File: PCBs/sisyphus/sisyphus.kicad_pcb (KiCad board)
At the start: 2 copper layers, 52 x 42 mm, 70 parts, among them J1 Light sensor, J10 Keyboard, J2 USB_C_Receptacle_USB2.0_14P, J3 AUX USB, J4 USB_BOOT, J5 Speaker, J6 Battery, J7 SWD, J8 Limit SW, J9 RGB_CONN, Q1 AO3401A, SW1 SW_SPDT_321, U1 TPS62293, U2 USBLC6-2P6, U3 BQ25619, U4 W25Q128JVS, U5 MAX98357A, U7 RP2040, Y1 ABM8-272-T3

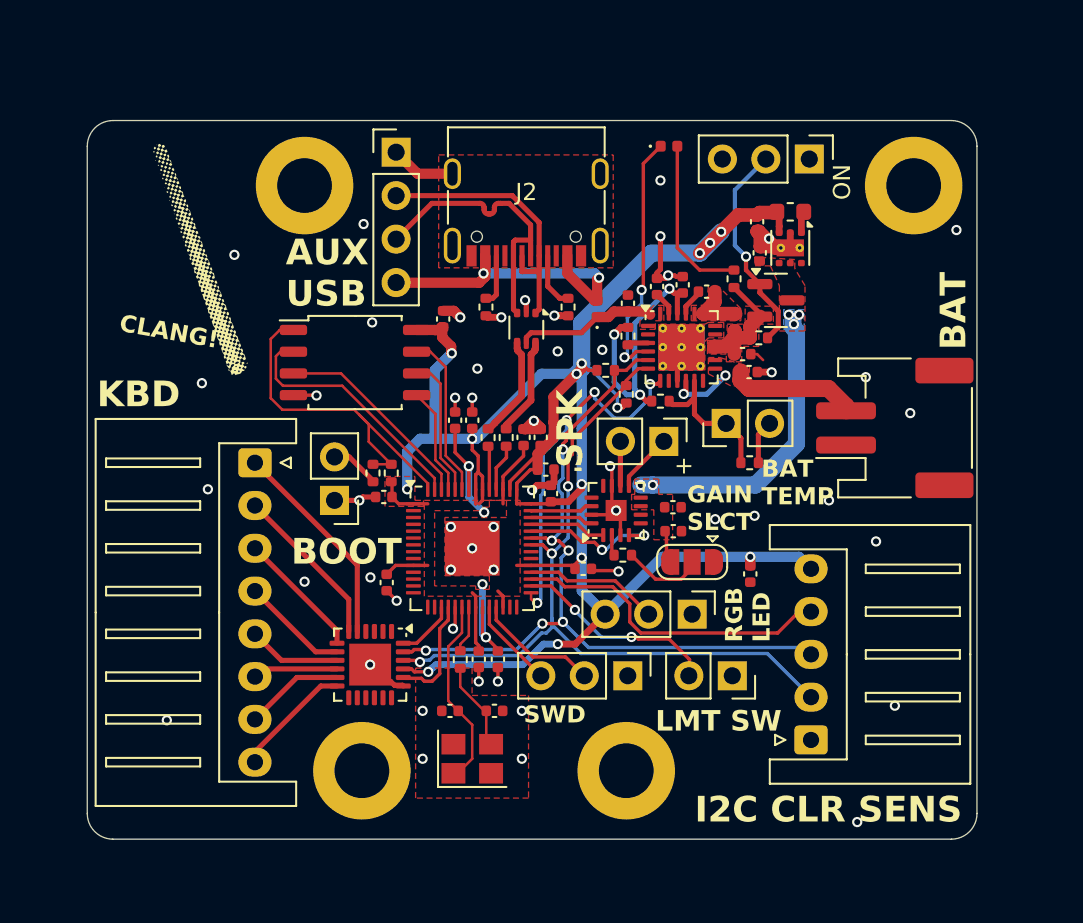
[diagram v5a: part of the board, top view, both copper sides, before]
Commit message: Fix things on PCB, update inductor size
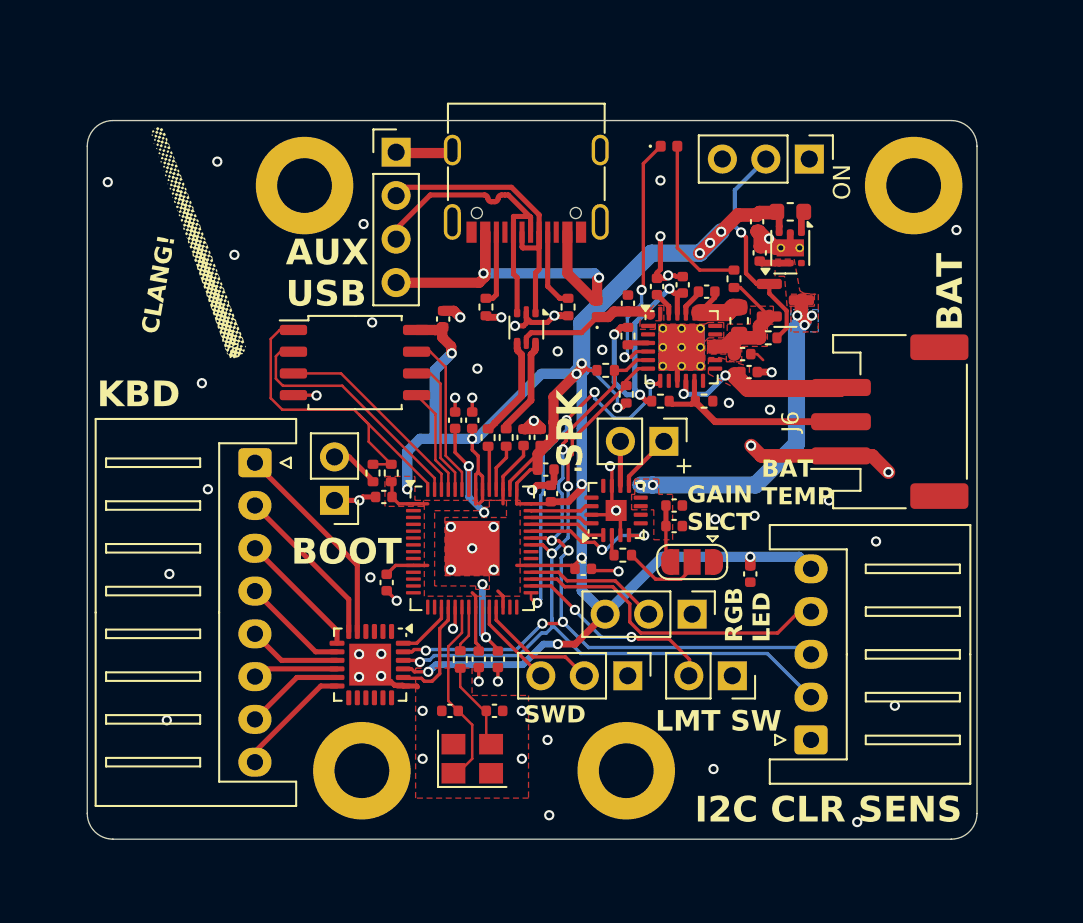
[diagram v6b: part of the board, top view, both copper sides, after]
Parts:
- removed TH1: 10k NTC, Connector_PinHeader_2.54mm:PinHeader_1x02_P2.54mm_Vertical
- J6: footprint Connector_JST:JST_PH_S2B-PH-SM4-TB_1x02-1MP_P2.00mm_Horizontal -> Connector_JST:JST_PH_S3B-PH-SM4-TB_1x03-1MP_P2.00mm_Horizontal
- L1: value 1uH -> 1uH 2A; footprint Inductor_SMD:L_0402_1005Metric -> Inductor_SMD:L_0603_1608Metric
- L2: value 2.2uH 1A -> 2.2uH 1.2A
- R8: value DNF -> 10k
- U8: value ~ -> TCA8418
- moved R7 4.48 mm to (113.5, 91.4)
- moved C10 1.50 mm to (111.8, 97.5)
- moved J2 1.38 mm to (103.2, 77.8)
- moved C9 1.10 mm to (111.8, 98.7)
- moved Q1 0.55 mm to (118.3, 85.5)
- moved R1 0.55 mm to (117.3, 87.7)
- moved J6 0.47 mm to (124.4, 92.6)
- moved L1 0.27 mm to (115.6, 86.7)
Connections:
- J6 pad 2: +BATT -> /Batery and power/NTC
- R6 pad 2: Net-(U3-TS) -> /Batery and power/NTC
- R7 pad 1: Net-(U3-TS) -> /Batery and power/NTC
- U3 pad 11: Net-(U3-TS) -> /Batery and power/NTC
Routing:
- net /Batery and power/NTC: track 0.00 -> 11.9 mm
- net GND: track 45.8 -> 55.3 mm, vias 52 -> 62
- net Net-(U3-TS): track 8.41 -> 0.00 mm
- net VSYS: track 19.4 -> 23.9 mm
- net VBUS: track 19.3 -> 23.4 mm
- net /Peripheral/DN: track 16.4 -> 17.8 mm
- net Net-(J2-CC1): track 3.26 -> 4.64 mm
- net Net-(J2-CC2): track 2.97 -> 4.35 mm
- net +BATT: track 11.2 -> 10.3 mm
- net SYS: track 8.74 -> 9.58 mm
- net /Peripheral/DP: track 17.1 -> 17.9 mm
- net Net-(Q1-G): track 12.5 -> 13.1 mm
- net /Batery and power/SW: track 3.49 -> 4.03 mm
- removed copper zone on F.Cu, net /Batery and power/SW

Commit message: Update things for that rendering F L A R E
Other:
- board text added: "NTC"
- board text removed: "BAT TEMP"

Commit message: Add the first actually ordered version of the PCB
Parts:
- removed the R6 at (111.0, 91.4)
- removed the R7 at (113.5, 91.4)
- added R11: 10k, Resistor_SMD:R_0402_1005Metric, F.Cu at (111.0, 91.3)
- D1: renamed from D2; footprint LED_SMD:LED_0402_1005Metric -> LED_SMD:LED_0603_1608Metric
- D2: renamed from D1; value D_Schottky -> D_shottky; footprint Diode_SMD:D_0402_1005Metric -> Diode_SMD:D_SOD-123
- L2: footprint Inductor_SMD:L_0603_1608Metric -> Inductor_SMD:L_0805_2012Metric
- R3: renamed from R11; value 27 -> 33
- R4: renamed from R12; value 27 -> 33
- R9: renamed from R4; value 220 -> 330
- U3: renamed from U1; value TPS62293 -> TPS62291
- moved C20 2.62 mm to (119.2, 80.2), turned to 90 degrees
- moved L2 2.18 mm to (120.7, 80.8), turned to -90 degrees
- moved D1 0.45 mm to (111.0, 76.5)
- renumbered C20 to C1, C13 to C10, C22 to C11, C21 to C12, C26 to C13, C23 to C14, C24 to C15, C1 to C16, C2 to C17, C3 to C18, C4 to C19, C19 to C2, C5 to C20, C6 to C21, C7 to C22, C8 to C23, C9 to C24, C10 to C25, C18 to C3, C17 to C4, C16 to C5, C15 to C6, C14 to C7, C11 to C8, C12 to C9, H4 to H1, H3 to H2, H2 to H3, H1 to H4, J4 to J1, J5 to J10, J7 to J2, J6 to J3, J2 to J4, J10 to J5, J3 to J6, J1 to J7, R8 to R1, R5 to R10, R2 to R12, R3 to R13, R10 to R14, R9 to R2, R13 to R5, R14 to R6, R15 to R7, R1 to R8, U4 to U1, U7 to U2, U3 to U4, U2 to U5, U8 to U6, U5 to U7
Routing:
- net VBUS: track 23.4 -> 20.5 mm
- net +3V3: track 130.4 -> 133.1 mm
- net GND: track 55.3 -> 57.2 mm, vias 62 -> 61
- net /Batery and power/NTC: track 11.9 -> 12.7 mm
- net Net-(U3-SW): track 1.23 -> 1.84 mm
